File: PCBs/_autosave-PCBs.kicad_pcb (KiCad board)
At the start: 4 copper layers, 29.8 x 11.3 mm, 8 parts, among them U6 TPS62172DSG

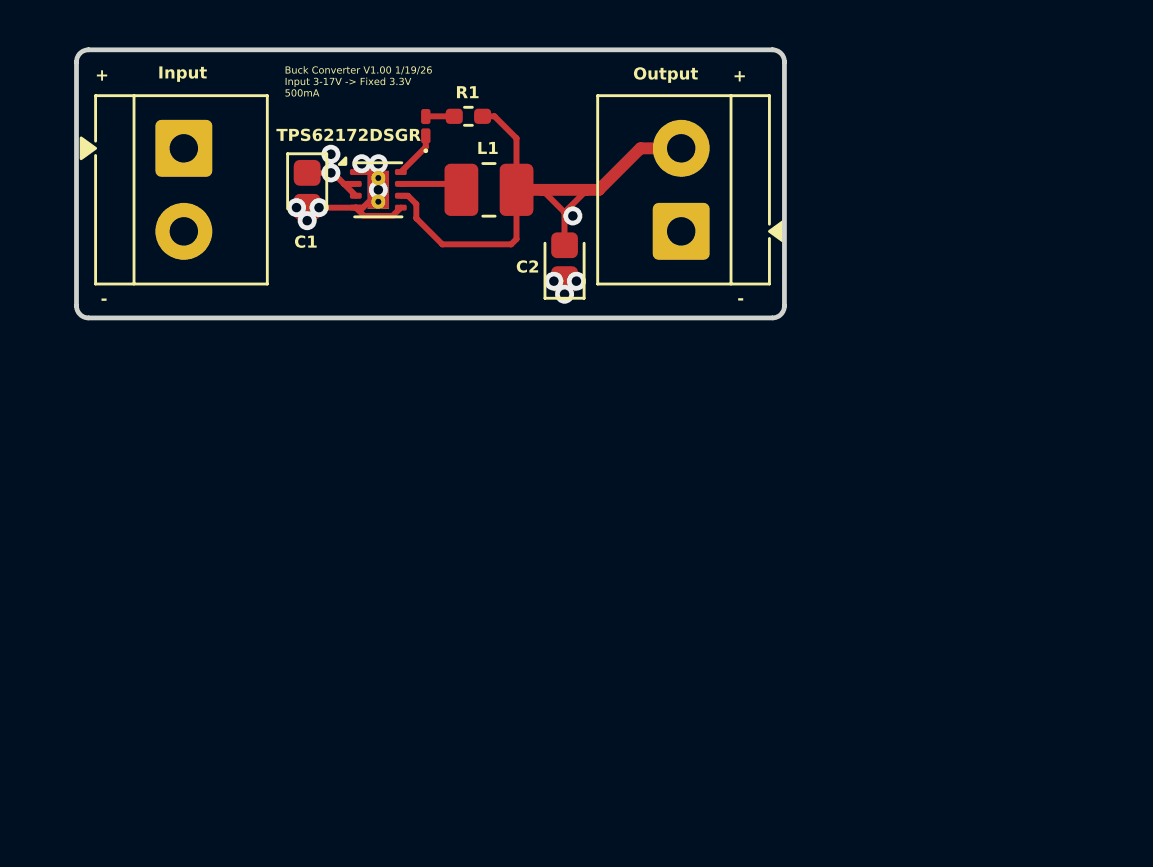
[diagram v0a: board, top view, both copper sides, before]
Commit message: changes for easyeda components
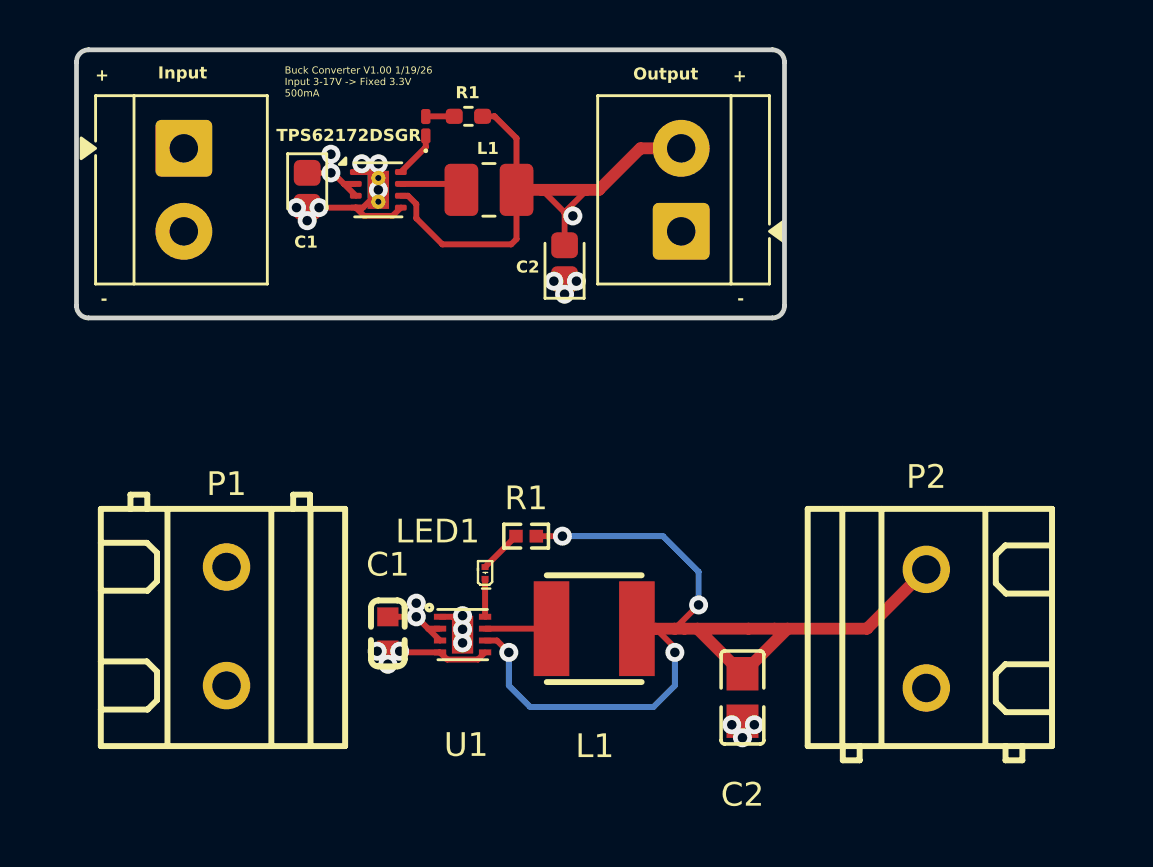
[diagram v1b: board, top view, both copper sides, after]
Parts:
- added C1: 10 uF, EasyEDA2KicadFootprints:C0603, F.Cu at (143.3, 114.9)
- added C2: 22 uF, EasyEDA2KicadFootprints:C0805, F.Cu at (158.2, 117.6)
- added L1: 2.2uH, EasyEDA2KicadFootprints:IND-SMD_L4.0-W4.0_LQH44PN2R2MP0L, F.Cu at (152.0, 114.7)
- added LED1: Green LED, EasyEDA2KicadFootprints:LED-SMD_L0.7-W0.4-RD_GREEN, F.Cu at (147.4, 112.3)
- added P1: Input 1x2, EasyEDA2KicadFootprints:CONN-TH_2P-P5.00_WJ128V-5.0-2P, F.Cu at (136.5, 114.6)
- added P2: Output 1x2, EasyEDA2KicadFootprints:CONN-TH_2P-P5.00_WJ128V-5.0-2P, F.Cu at (166.0, 114.7)
- added R1: 100k Ohms, EasyEDA2KicadFootprints:R0402, F.Cu at (149.1, 110.8)
- added U1: TPS62172DSGR, EasyEDA2KicadFootprints:WSON-8_L2.0-W2.0-P0.50-TL-EP, F.Cu at (146.4, 115.0)
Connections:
- BuckConverter3-17V->3.3V-ScrewTerminalInput1 pad 1: VCCIN -> unconnected-(BuckConverter3-17V->3.3V-ScrewTerminalInput1-Pin_1-Pad1)
- BuckConverter3-17V->3.3V-ScrewTerminalInput1 pad 2: GND -> unconnected-(BuckConverter3-17V->3.3V-ScrewTerminalInput1-Pin_2-Pad2)
- BuckConverter3-17V->3.3V-ScrewTerminalOutput1 pad 1: GND -> unconnected-(BuckConverter3-17V->3.3V-ScrewTerminalOutput1-Pin_1-Pad1)
- BuckConverter3-17V->3.3V-ScrewTerminalOutput1 pad 2: VCCOUT -> unconnected-(BuckConverter3-17V->3.3V-ScrewTerminalOutput1-Pin_2-Pad2)
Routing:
- net VCCOUT: track 24.0 -> 67.2 mm, vias 1 -> 5
- net GND: track 7.65 -> 13.5 mm, vias 9 -> 18
- net VCCIN: track 3.95 -> 7.26 mm, vias 2 -> 4
- net Net-(U1-SW): track 0.00 -> 2.80 mm
- net Net-(LED1-A): track 0.00 -> 1.84 mm
- net Net-(LED1-K): track 0.00 -> 1.60 mm

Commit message: should be done
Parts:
- removed BuckConverter3-17V->3.3V-C1: 10uF, Capacitor_Tantalum_SMD:CP_EIA-1608-10_AVX-L
- removed BuckConverter3-17V->3.3V-C2: 22uF, Capacitor_Tantalum_SMD:CP_EIA-1608-10_AVX-L
- removed BuckConverter3-17V->3.3V-L1: 2.2 uH, Inductor_SMD:L_1008_2520Metric_Pad1.43x2.20mm_HandSolder
- removed BuckConverter3-17V->3.3V-LED1: LED, LED_SMD:LED_0201_0603Metric_Pad0.64x0.40mm_HandSolder
- removed BuckConverter3-17V->3.3V-R1: 100k Ohms, Resistor_SMD:R_0402_1005Metric_Pad0.72x0.64mm_HandSolder
- removed BuckConverter3-17V->3.3V-ScrewTerminalInput1: Input, TerminalBlock_4Ucon:TerminalBlock_4Ucon_1x02_P3.50mm_Horizontal
- removed BuckConverter3-17V->3.3V-ScrewTerminalOutput1: Output, TerminalBlock_4Ucon:TerminalBlock_4Ucon_1x02_P3.50mm_Horizontal
- removed U6: TPS62172DSG, Package_SON:WSON-8-1EP_2x2mm_P0.5mm_EP0.9x1.6mm_ThermalVias
- moved P1 0.10 mm to (136.4, 114.6)
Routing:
- net VCCOUT: track 67.2 -> 43.2 mm, vias 5 -> 4
- net GND: track 13.5 -> 7.69 mm, vias 18 -> 9
- net VCCIN: track 7.26 -> 3.31 mm, vias 4 -> 2
- net Net-(U6-SW): track 2.65 -> 0.00 mm
- net Net-(BuckConverter3-17V->3.3V-LED1-K): track 1.96 -> 0.00 mm
- net Net-(BuckConverter3-17V->3.3V-LED1-A): track 1.20 -> 0.00 mm
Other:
- board size 29.8 x 11.3 mm -> 44.5 x 15.5 mm
- board text removed: "C1"
- board text removed: "C2"
- board text removed: "Input"
- board text removed: "L1"
- board text removed: "Output"
- board text removed: "R1"
- board text removed: "TPS62172DSGR"
